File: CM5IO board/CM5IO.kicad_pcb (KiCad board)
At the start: 4 copper layers, 160 x 90 mm, 66 parts, among them J11 USB_C_Receptacle_USB2.0, J12 USB3_A, J14 JST_SHBM04B-SRSS-TB, J16 Conn_01x22_Female, J2 Conn_02x07_Odd_Even, J3 Conn_01x03, J4 Bus_M.2_Socket_M, J5 Conn_01x22_Female, J6 THD-02-R, J7 Micro_SD_Card_Det, J8 THD-20-R, SW1 Right angle Tact button, U18 RT9742GGJ5, U6 AP22653W6, U7 ASEK-32.768KHZ-L-R-T, U8 AP3441SHE-7B

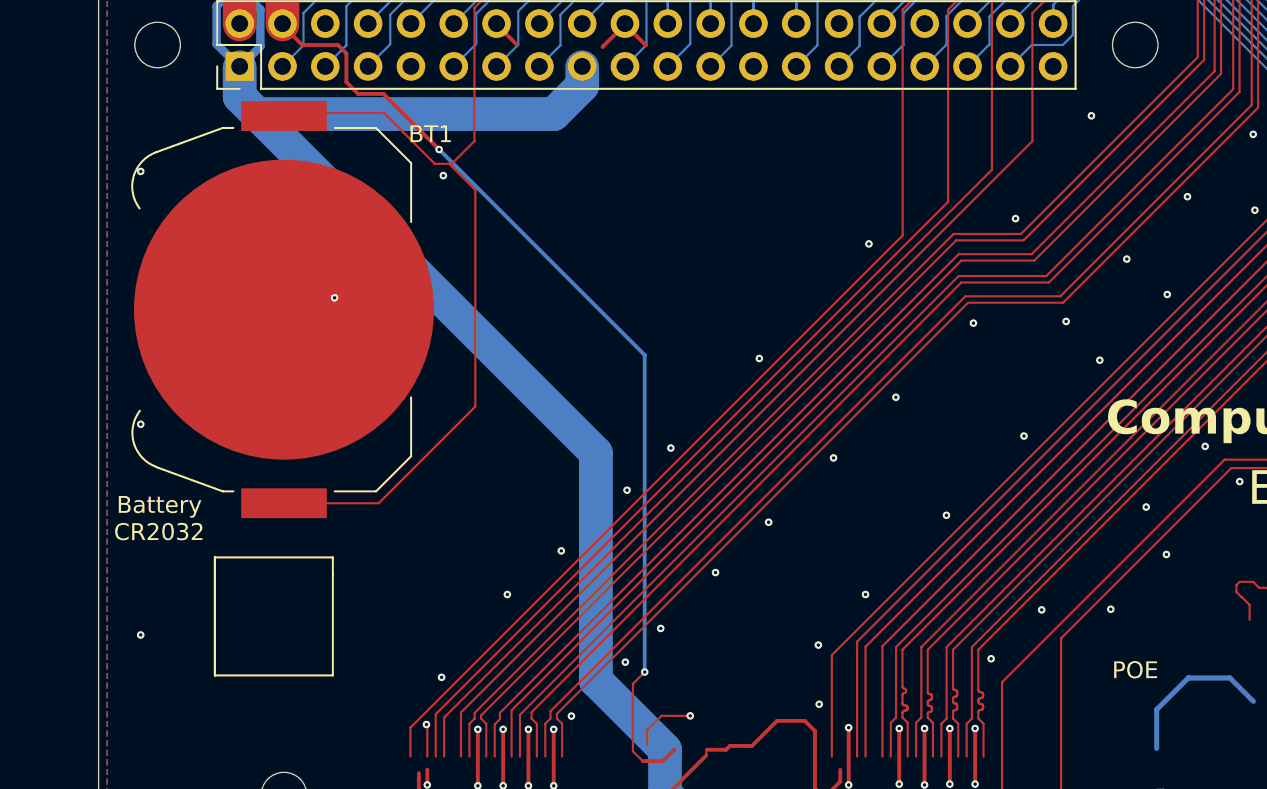
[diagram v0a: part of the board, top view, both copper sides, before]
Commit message: Copied Ricardo template on CM5IO board
There's not enough space!!
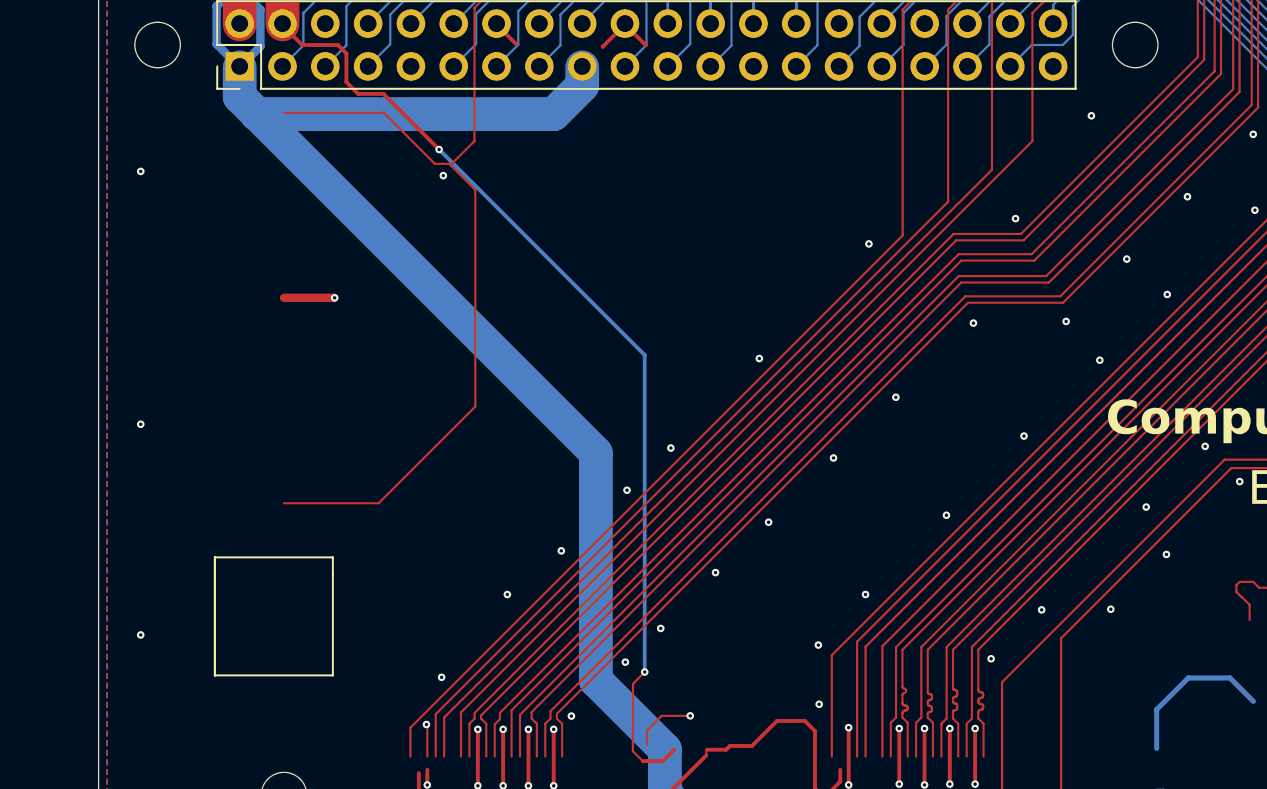
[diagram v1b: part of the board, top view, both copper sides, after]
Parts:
- removed BT1: Battery_Cell, CM5IO:BatteryHolder_Keystone_3034_1x20mm
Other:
- board text removed: "Battery CR2032"
- board text removed: "POE"

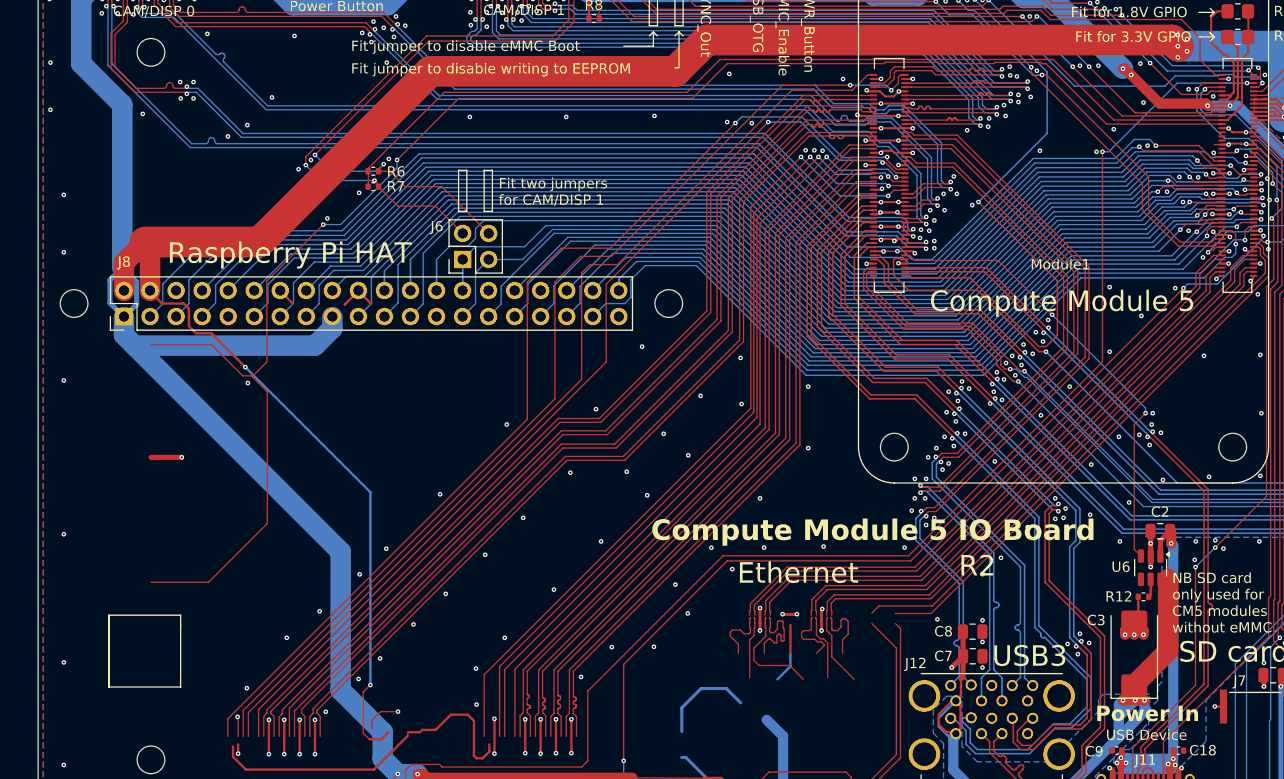
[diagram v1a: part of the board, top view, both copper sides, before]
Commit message: Blocked off vbat
still need to block off ethernet
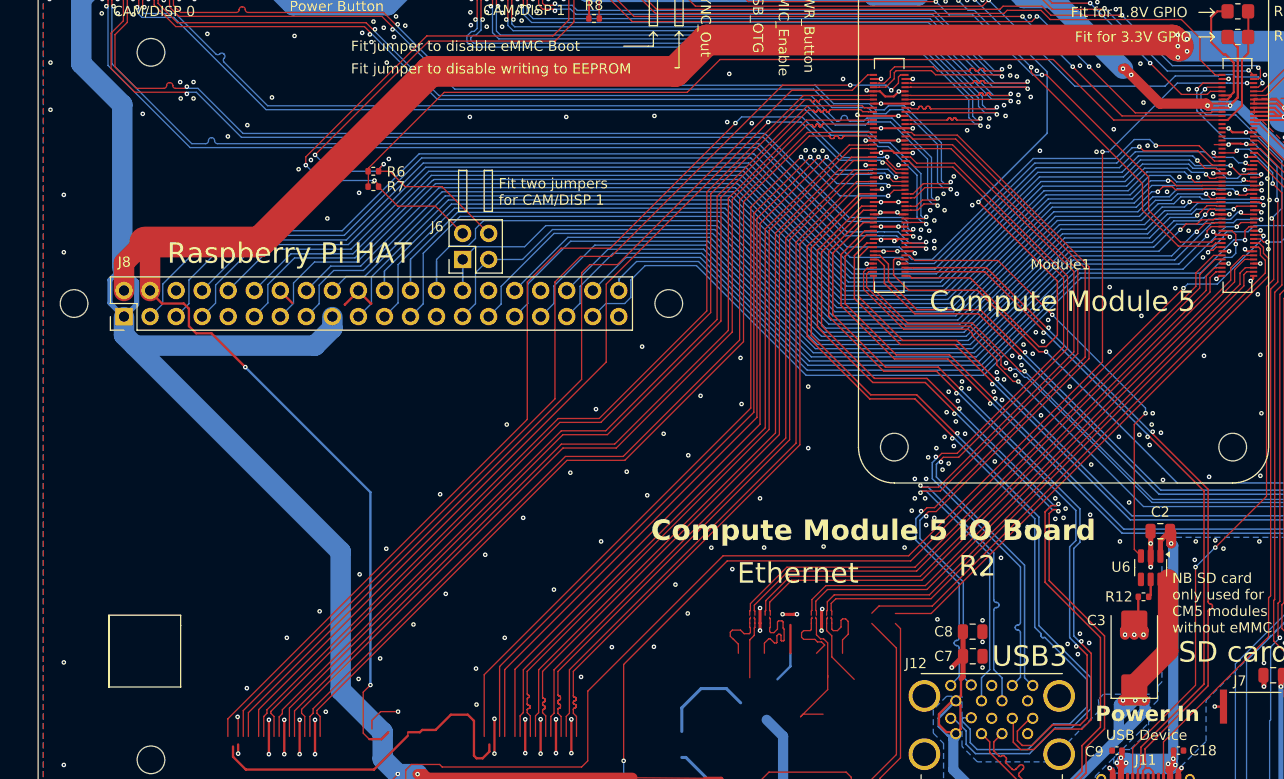
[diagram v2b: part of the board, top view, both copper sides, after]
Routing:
- net /CM5_GPIO ( Ethernet, GPIO, SDCARD)/VBAT: track 154.8 -> 0.00 mm, vias 2 -> 0
- net /CM5_GPIO ( Ethernet, GPIO, SDCARD)/TRD1_N: track 10.3 -> 0.00 mm
- net /CM5_GPIO ( Ethernet, GPIO, SDCARD)/TRD2_N: track 6.55 -> 13.9 mm
- net GND: track 759.2 -> 756.2 mm, vias 468 -> 464
